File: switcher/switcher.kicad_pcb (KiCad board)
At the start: 2 copper layers, 65.4 x 109.2 mm, 37 parts, among them J2 Conn_01x18, J3_LED1 Conn_02x08_Odd_Even, K0 HFD2_005-S-L2-D, K1 HFD2_005-S-L2-D, K2 HFD2_005-S-L2-D, U1 INA3221_Module, U2 ULN2803A, U3 ULN2803A, U5 MCP2551-I-P, U6 ChinaBluePill-bluepill-D3_Boa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

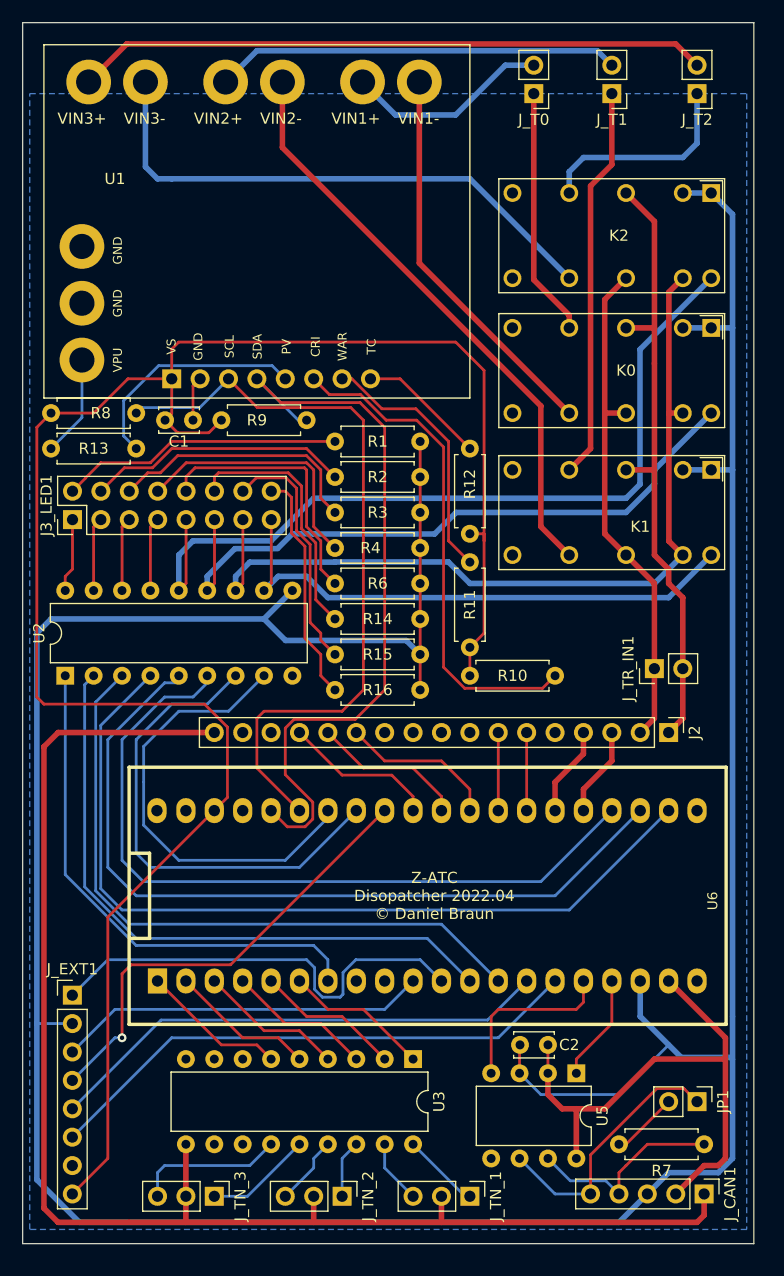
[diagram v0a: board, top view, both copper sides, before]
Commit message: add switcher board, derived from dispatcher
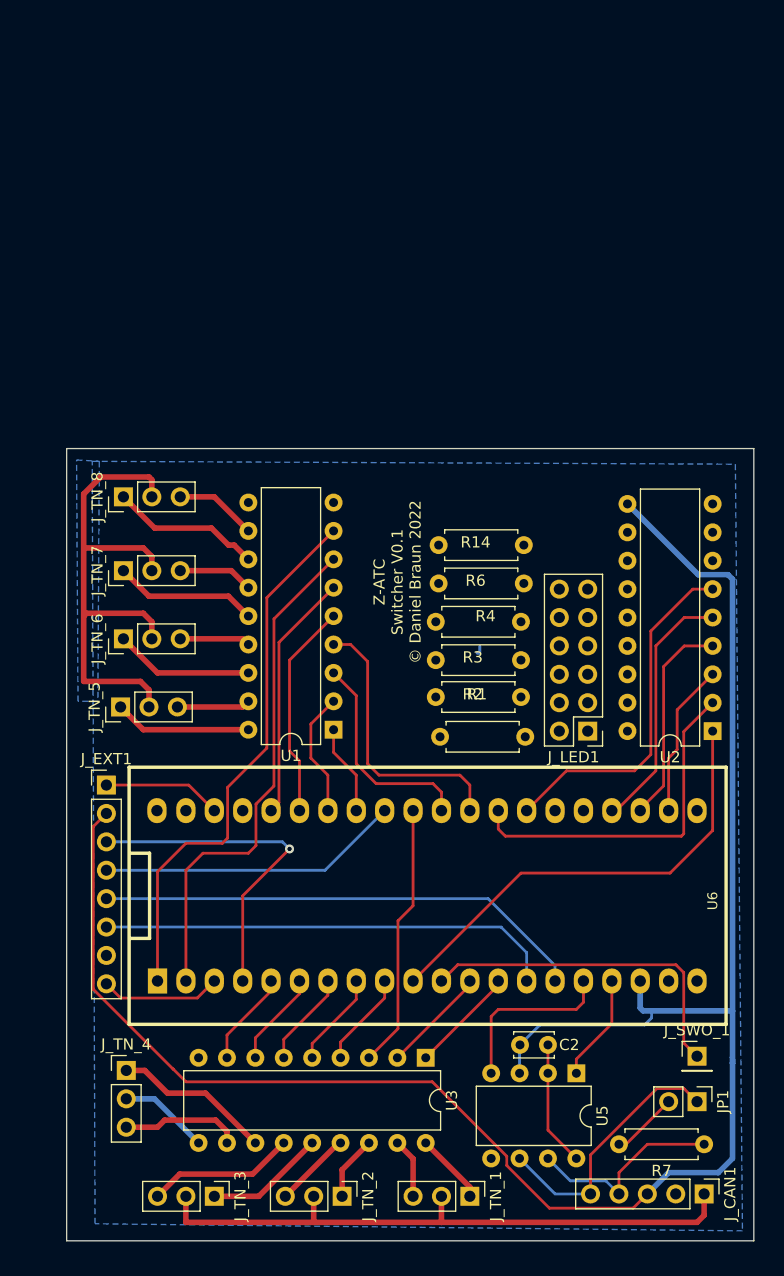
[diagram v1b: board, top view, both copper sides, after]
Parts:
- removed C1: C, Capacitor_THT:C_Disc_D3.4mm_W2.1mm_P2.50mm
- removed J2: Conn_01x18, Connector_PinHeader_2.54mm:PinHeader_1x17_P2.54mm_Vertical
- removed J3_LED1: Conn_02x08_Odd_Even, Connector_PinHeader_2.54mm:PinHeader_2x08_P2.54mm_Vertical
- removed J_T0, J_T1, J_T2, J_TR_IN1: Conn_01x02_Female, Connector_PinHeader_2.54mm:PinHeader_1x02_P2.54mm_Vertical
- removed K0, K1, K2: HFD2_005-S-L2-D, Modules:HFD2-005-S-L2-D
- removed R10, R11, R12, R13, R8, R9: 10k, Resistor_THT:R_Axial_DIN0207_L6.3mm_D2.5mm_P7.62mm_Horizontal
- removed R15, R16: R, Resistor_THT:R_Axial_DIN0207_L6.3mm_D2.5mm_P7.62mm_Horizontal
- added J_LED1: Conn_02x06_Odd_Even, Connector_PinHeader_2.54mm:PinHeader_2x06_P2.54mm_Vertical, F.Cu at (122.9, 126.2)
- added J_SWO_1: Conn_01x01_Female, Connector_PinHeader_2.54mm:PinHeader_1x01_P2.54mm_Vertical, F.Cu at (132.7, 155.3)
- added J_TN_4: Conn_01x03_Female, Connector_PinHeader_2.54mm:PinHeader_1x03_P2.54mm_Vertical, F.Cu at (81.7, 156.6)
- added J_TN_5: Conn_01x03_Female, Connector_PinHeader_2.54mm:PinHeader_1x03_P2.54mm_Vertical, F.Cu at (81.2, 124.1)
- added J_TN_6: Conn_01x03_Female, Connector_PinHeader_2.54mm:PinHeader_1x03_P2.54mm_Vertical, F.Cu at (81.4, 118.0)
- added J_TN_7: Conn_01x03_Female, Connector_PinHeader_2.54mm:PinHeader_1x03_P2.54mm_Vertical, F.Cu at (81.4, 111.9)
- added J_TN_8: Conn_01x03_Female, Connector_PinHeader_2.54mm:PinHeader_1x03_P2.54mm_Vertical, F.Cu at (81.4, 105.3)
- U1: value INA3221_Module -> ULN2803A; footprint jwm_kicad_footprints_misc:INA3221_Module -> Package_DIP:DIP-18_W7.62mm
- moved U2 58.1 mm to (134.1, 126.2), turned to 180 degrees
- moved U1 34.6 mm to (100.2, 126.1)
- moved R1 26.5 mm to (109.7, 126.7), turned to 0 degrees
- moved R2 19.7 mm to (109.3, 123.2), turned to 0 degrees
- moved J_EXT1 19.0 mm to (79.9, 131.1)
- moved R3 13.3 mm to (109.3, 119.9), turned to 0 degrees
- moved R14 6.81 mm to (109.6, 109.6), turned to 0 degrees
- moved R4 6.75 mm to (109.3, 116.5), turned to 0 degrees
- moved R6 1.65 mm to (109.6, 113.0), turned to 0 degrees
- moved U3 1.14 mm to (108.4, 155.5)
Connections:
- J_EXT1 pad 1: SWO -> +3V3
- J_EXT1 pad 3: TRIG -> X2
- J_EXT1 pad 5: SCL1 -> SDA1
- J_EXT1 pad 6: SDA1 -> SCL1
- J_EXT1 pad 8: +3V3 -> X1
- U1 pad 1: +3V3 -> TURN5A
- U1 pad 10: T0_1 -> +12V
- U1 pad 11: TT1_1 -> Net-(J_TN_8-Pad3)
- U1 pad 12: T1_1 -> Net-(J_TN_8-Pad1)
- U1 pad 13: TT2_1 -> Net-(J_TN_7-Pad3)
- U1 pad 14: T2_1 -> Net-(J_TN_7-Pad1)
- U1 pad 2: GND -> TURN5B
- U1 pad 3: SCL2 -> TURN6A
- U1 pad 4: SDA2 -> TURN6B
- U1 pad 5: Net-(R13-Pad2) -> TURN7A
- U1 pad 6: Net-(R10-Pad2) -> TURN7B
- U1 pad 7: Net-(R11-Pad2) -> TURN8A
- U1 pad 8: Net-(R12-Pad1) -> TURN8B
- U1 pad 9: TT0_1 -> GND
- U2 pad 11: Net-(J3_LED1-Pad15) -> unconnected-(U2-Pad11)
- U2 pad 12: Net-(J3_LED1-Pad13) -> unconnected-(U2-Pad12)
- U2 pad 5: RELAY_SET2 -> LED4
- U2 pad 6: RELAY_SET0 -> LED5
- U2 pad 7: RELAY0 -> unconnected-(U2-Pad7)
- U2 pad 8: RELAY_SET1 -> unconnected-(U2-Pad8)
- U3 pad 11: unconnected-(U3-Pad11) -> Net-(U3-Pad11)
- U3 pad 12: unconnected-(U3-Pad12) -> Net-(U3-Pad12)
- U3 pad 7: unconnected-(U3-Pad7) -> TURN4A
- U3 pad 8: unconnected-(U3-Pad8) -> TURN4B
- U6 pad 1: TURN3B -> TURN8B
- U6 pad 10: TRIG -> LED0
- U6 pad 12: LED1 -> TURN1B
- U6 pad 13: LED2 -> TURN1A
- U6 pad 2: TURN3A -> TURN8A
- U6 pad 22: LED3 -> LED2
- U6 pad 23: RELAY_SET2 -> LED3
- U6 pad 24: RELAY_SET0 -> LED4
- U6 pad 27: PWM0_1 -> LED5
- U6 pad 28: PWM0_2 -> LED1
- U6 pad 29: CT_0_1 -> TURN6B
- U6 pad 3: TURN2B -> X1
- U6 pad 30: CT_0_2 -> TURN6A
- U6 pad 31: CT_0_3 -> TURN2A
- U6 pad 33: RELAY0 -> TURN5A
- U6 pad 34: RELAY_SET1 -> TURN5B
- U6 pad 35: SCL2 -> TURN7A
- U6 pad 36: SDA2 -> TURN7B
- U6 pad 4: TURN2A -> X2
- U6 pad 5: TURN1B -> TURN4B
- U6 pad 6: TURN1A -> TURN4A
- U6 pad 7: LED0 -> TURN3B
- U6 pad 8: USB1 -> TURN3A
- U6 pad 9: USB2 -> TURN2B
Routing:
- net +3V3: track 175.2 -> 10.6 mm
- net +5V: track 310.3 -> 175.2 mm
- net Net-(J3_LED1-Pad13): track 77.3 -> 0.00 mm
- net Net-(U2-Pad14): track 74.7 -> 0.00 mm
- net RELAY_SET2: track 72.4 -> 0.00 mm
- net RELAY_SET0: track 68.4 -> 0.00 mm
- net SCL2: track 67.7 -> 0.00 mm
- net SDA2: track 66.8 -> 0.00 mm
- net Net-(U2-Pad13): track 59.7 -> 0.00 mm
- net LED3: track 76.2 -> 18.9 mm
- net T2_1: track 56.6 -> 0.00 mm
- net TRACK0_0: track 56.0 -> 0.00 mm
- net TT1_1: track 52.9 -> 0.00 mm
- net TT2_1: track 49.6 -> 0.00 mm
- net Net-(J3_LED1-Pad15): track 49.5 -> 0.00 mm
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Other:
- board size 65.4 x 109.2 mm -> 61.5 x 70.9 mm
- board text added: "Z-ATC Switcher V0.1 © Daniel Braun 2022"
- board text removed: "Z-ATC Disopatcher 2022.04 © Daniel Braun"

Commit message: update switcher board, DRC OK
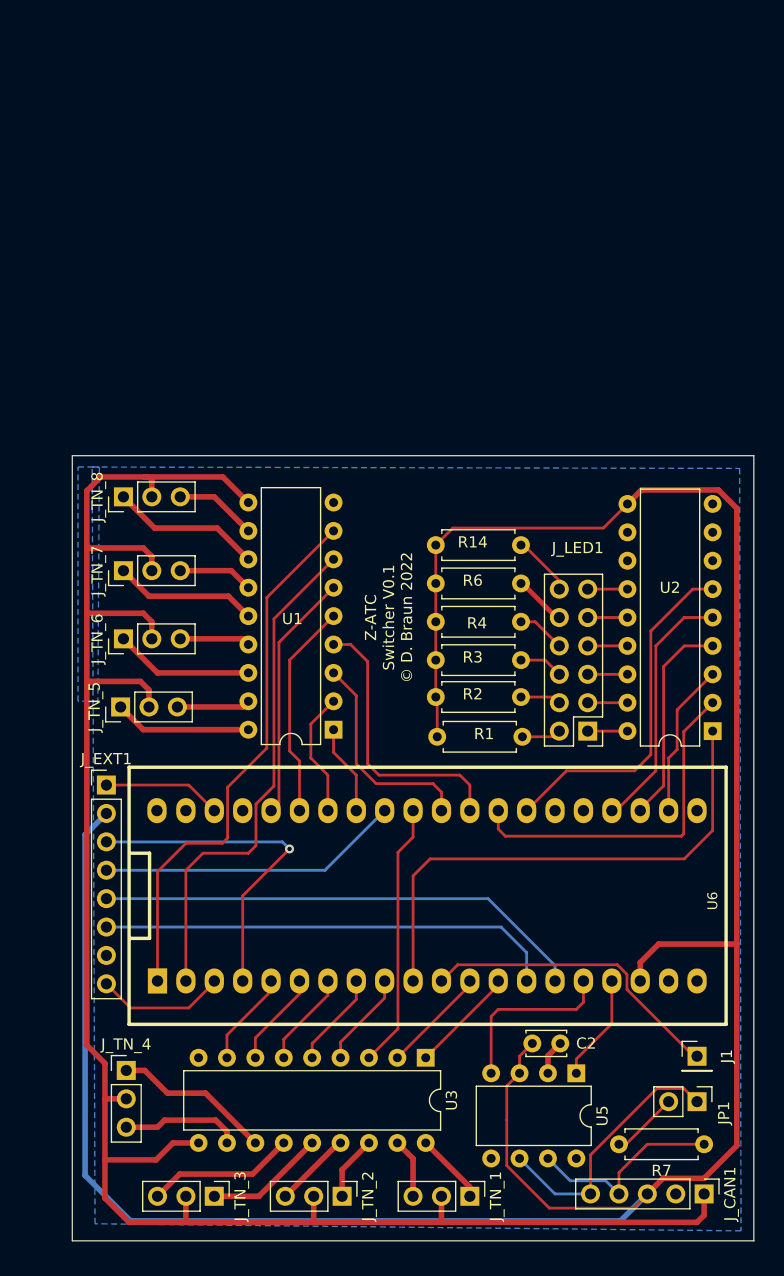
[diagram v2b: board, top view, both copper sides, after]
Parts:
- moved C2 1.11 mm to (120.5, 154.2)
- moved R14 0.25 mm to (109.3, 109.6)
- moved R6 0.25 mm to (109.3, 113.0)
- moved R1 0.25 mm to (109.5, 126.7)
- renumbered J_SWO_1 to J1
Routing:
- net +12V: track 112.1 -> 179.6 mm
- net +5V: track 175.2 -> 237.3 mm
- net Net-(R6-Pad2): track 0.00 -> 9.13 mm
- net GND: track 11.2 -> 3.12 mm
- net Net-(R14-Pad2): track 0.00 -> 5.51 mm
- net LED0: track 41.3 -> 46.8 mm
- net Net-(R4-Pad2): track 0.00 -> 4.32 mm
- net Net-(R3-Pad2): track 0.00 -> 3.96 mm
- net Net-(R2-Pad2): track 0.00 -> 3.64 mm
- net Net-(U2-Pad18): track 0.00 -> 3.56 mm
- net Net-(U2-Pad17): track 0.00 -> 3.56 mm
- net Net-(U2-Pad16): track 0.00 -> 3.56 mm
- net Net-(U2-Pad15): track 0.00 -> 3.56 mm
- net Net-(U2-Pad14): track 0.00 -> 3.56 mm
- net Net-(U2-Pad13): track 0.00 -> 3.56 mm
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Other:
- board size 61.5 x 70.9 mm -> 61 x 70.2 mm
- board text added: "Z-ATC Switcher V0.1 © D. Braun 2022"
- board text removed: "Z-ATC Switcher V0.1 © Daniel Braun 2022"

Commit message: ..
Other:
- board size 61 x 70.2 mm -> 62.2 x 71.4 mm
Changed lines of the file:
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@@
       (layerselection 0x00010fc_ffffffff)
       (disableapertmacros false)
-      (usegerberextensions false)
-      (usegerberattributes true)
-      (usegerberadvancedattributes true)
-      (creategerberjobfile true)
+      (usegerberextensions true)
+      (usegerberattributes false)
+      (usegerberadvancedattributes false)
+      (creategerberjobfile false)
       (svguseinch false)
       (svgprecision 6)
@@
       (psa4output false)
       (plotreference true)
-      (plotvalue true)
+      (plotvalue false)
       (plotinvisibletext false)
       (sketchpadsonfab false)
-      (subtractmaskfromsilk false)
+      (subtractmaskfromsilk true)
       (outputformat 1)
       (mirror false)
-      (drillshape 1)
+      (drillshape 0)
       (scaleselection 1)
-      (outputdirectory "")
+      (outputdirectory "../gerber/switcherv1/")
     )
   )
@@
     )
   )
-  (gr_rect (start 137.795 171.831) (end 76.835 101.6) (layer "Edge.Cuts") (width 0.05) (fill none))
+  (gr_rect (start 138.43 172.974) (end 76.2 101.6) (layer "Edge.Cuts") (width 0.05) (fill none))
   (gr_text "Z-ATC\nSwitcher V0.1\n© D. Braun 2022" (at 105.156 116.078 90) (layer "F.SilkS")
     (effects (font (size 1 1) (thickness 0.15)))
